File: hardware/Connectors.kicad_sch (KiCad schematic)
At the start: 23 parts, among them J1 USB_C_Receptacle_USB2.0, J14 Conn_01x05, J2 M80-5302642, J3 M300-MV31045M1, J4 M80-5L10442MC, J5 M80-5L10442MC, J6 M80-5L10442MC, J7 M80-5L10442MC

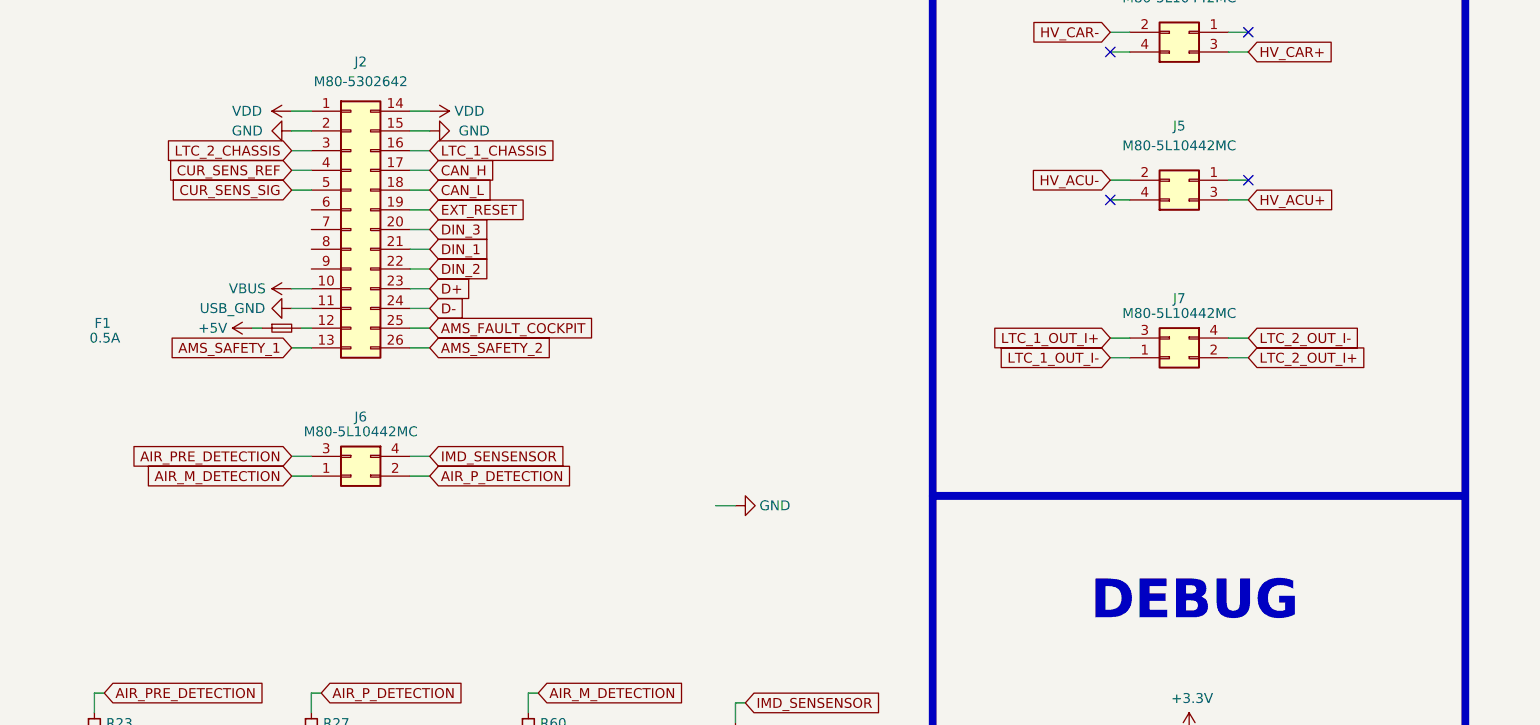
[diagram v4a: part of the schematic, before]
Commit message: bigger board, distinct HV/LV and isolation, some schematic changes
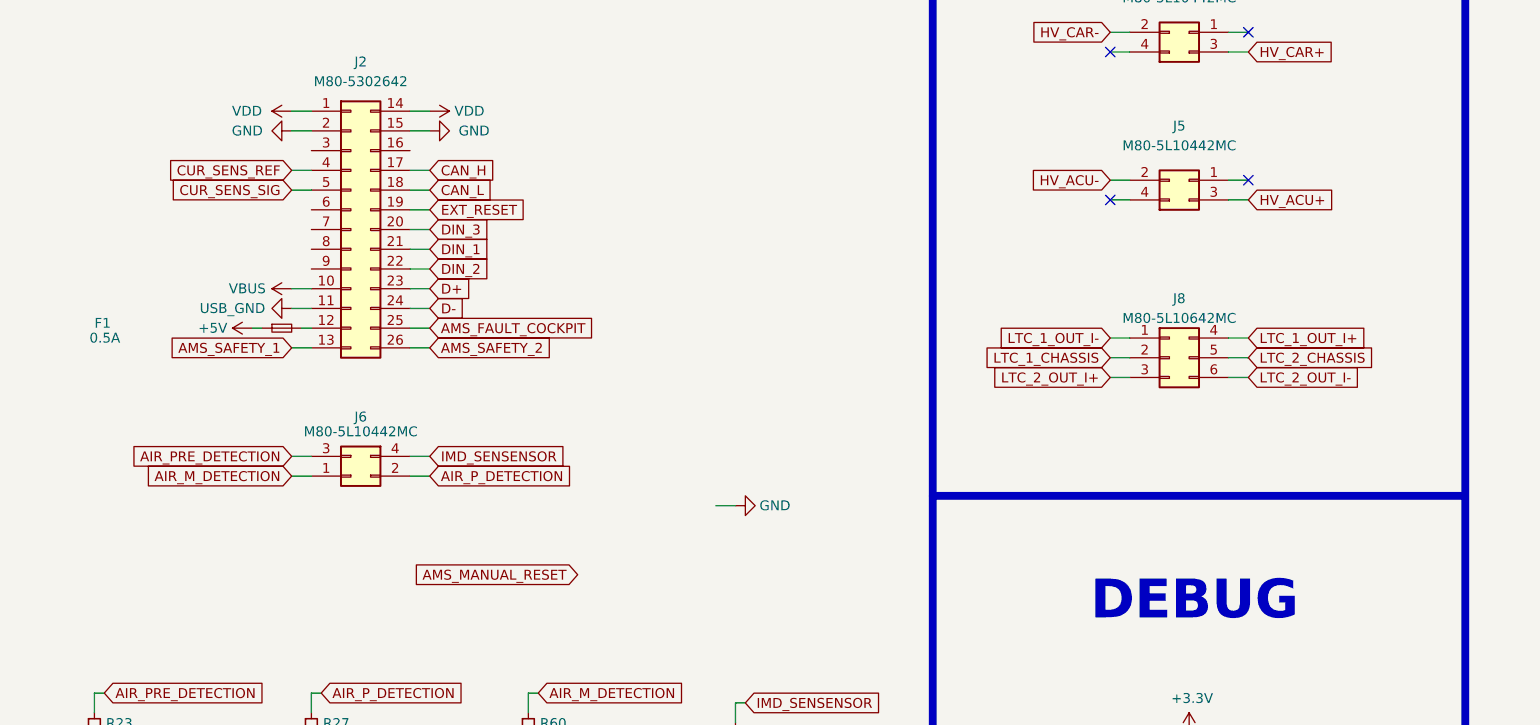
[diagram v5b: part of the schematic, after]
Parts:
- removed J7: M80-5L10442MC, M80-5L104YYMC, symbol M80-5L10442MC:M80-5L10442MC
- added J8: M80-5L10642MC, M80-5L10642MC:M80-5L106YYMC, symbol M80-5L10642MC:M80-5L10642MC
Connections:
- net LTC_1_CHASSIS: now also J8.2; no longer J2.16
- net LTC_1_OUT_I+: now also J8.4
- net LTC_1_OUT_I-: now also J8.1
- net LTC_2_CHASSIS: now also J8.5; no longer J2.3
- net LTC_2_OUT_I+: now also J8.3
- net LTC_2_OUT_I-: now also J8.6
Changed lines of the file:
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@@
     (stroke (width 0) (type default))
   )
-  (wire (pts (xy 170.18 83.82) (xy 172.72 83.82))
+  (wire (pts (xy 170.18 81.28) (xy 172.72 81.28))
     (stroke (width 0) (type default))
   )
@@
     (stroke (width 0) (type default))
   )
-  (wire (pts (xy 64.77 57.15) (xy 67.31 57.15))
+  (wire (pts (xy 187.96 83.82) (xy 185.42 83.82))
     (stroke (width 0) (type default))
   )
@@
     (stroke (width 0) (type default))
   )
-  (wire (pts (xy 187.96 81.28) (xy 185.42 81.28))
+  (wire (pts (xy 187.96 86.36) (xy 185.42 86.36))
     (stroke (width 0) (type default))
   )
@@
     (stroke (width 0) (type default))
   )
-  (wire (pts (xy 170.18 81.28) (xy 172.72 81.28))
+  (wire (pts (xy 187.96 81.28) (xy 185.42 81.28))
     (stroke (width 0) (type default))
   )
@@
     (stroke (width 0) (type default))
   )
-  (wire (pts (xy 82.55 57.15) (xy 80.01 57.15))
+  (wire (pts (xy 170.18 83.82) (xy 172.72 83.82))
     (stroke (width 0) (type default))
   )
@@
     (stroke (width 0) (type default))
   )
-  (wire (pts (xy 187.96 83.82) (xy 185.42 83.82))
+  (wire (pts (xy 170.18 86.36) (xy 172.72 86.36))
     (stroke (width 0) (type default))
   )
@@
     )
   )
-  (global_label "LTC_1_OUT_I-" (shape input) (at 170.18 83.82 180) (fields_autoplaced)
-    (effects (font (size 1.27 1.27)) (justify right))
-    (property "Intersheetrefs" "${INTERSHEET_REFS}" (at 154.7446 83.82 0)
-      (effects (font (size 1.27 1.27)) (justify right) hide)
-    )
-  )
-  (global_label "LTC_1_CHASSIS" (shape input) (at 82.55 57.15 0) (fields_autoplaced)
-    (effects (font (size 1.27 1.27)) (justify left))
-    (property "Intersheetrefs" "${INTERSHEET_REFS}" (at 99.2071 57.2294 0)
-      (effects (font (size 1.27 1.27)) (justify left) hide)
+  (global_label "LTC_1_OUT_I-" (shape input) (at 170.18 81.28 180) (fields_autoplaced)
+    (effects (font (size 1.27 1.27)) (justify right))
+    (property "Intersheetrefs" "${INTERSHEET_REFS}" (at 154.7446 81.28 0)
+      (effects (font (size 1.27 1.27)) (justify right) hide)
+    )
+  )
+  (global_label "LTC_1_CHASSIS" (shape input) (at 170.18 83.82 180) (fields_autoplaced)
+    (effects (font (size 1.27 1.27)) (justify right))
+    (property "Intersheetrefs" "${INTERSHEET_REFS}" (at 153.5956 83.82 0)
+      (effects (font (size 1.27 1.27)) (justify right) hide)
     )
   )
@@
     )
   )
+  (global_label "AMS_MANUAL_RESET" (shape input) (at 101.6 111.76 180) (fields_autoplaced)
+    (effects (font (size 1.27 1.27)) (justify right))
+    (property "Intersheetrefs" "${INTERSHEET_REFS}" (at 80.6009 111.76 0)
+      (effects (font (size 1.27 1.27)) (justify right) hide)
+    )
+  )
   (global_label "DIN_1" (shape input) (at 82.55 69.85 0) (fields_autoplaced)
     (effects (font (size 1.27 1.27)) (justify left))
@@
     )
   )
-  (global_label "LTC_2_OUT_I+" (shape input) (at 187.96 83.82 0) (fields_autoplaced)
-    (effects (font (size 1.27 1.27)) (justify left))
-    (property "Intersheetrefs" "${INTERSHEET_REFS}" (at 203.3954 83.82 0)
-      (effects (font (size 1.27 1.27)) (justify left) hide)
+  (global_label "LTC_2_OUT_I+" (shape input) (at 170.18 86.36 180) (fields_autoplaced)
+    (effects (font (size 1.27 1.27)) (justify right))
+    (property "Intersheetrefs" "${INTERSHEET_REFS}" (at 154.7446 86.36 0)
+      (effects (font (size 1.27 1.27)) (justify right) hide)
     )
   )
@@
     )
   )
-  (global_label "LTC_1_OUT_I+" (shape input) (at 170.18 81.28 180) (fields_autoplaced)
-    (effects (font (size 1.27 1.27)) (justify right))
-    (property "Intersheetrefs" "${INTERSHEET_REFS}" (at 154.7446 81.28 0)
-      (effects (font (size 1.27 1.27)) (justify right) hide)
+  (global_label "LTC_1_OUT_I+" (shape input) (at 187.96 81.28 0) (fields_autoplaced)
+    (effects (font (size 1.27 1.27)) (justify left))
+    (property "Intersheetrefs" "${INTERSHEET_REFS}" (at 203.3954 81.28 0)
+      (effects (font (size 1.27 1.27)) (justify left) hide)
     )
   )
@@
     )
   )
-  (global_label "LTC_2_CHASSIS" (shape input) (at 64.77 57.15 180) (fields_autoplaced)
-    (effects (font (size 1.27 1.27)) (justify right))
-    (property "Intersheetrefs" "${INTERSHEET_REFS}" (at 48.1129 57.0706 0)
-      (effects (font (size 1.27 1.27)) (justify right) hide)
+  (global_label "LTC_2_CHASSIS" (shape input) (at 187.96 83.82 0) (fields_autoplaced)
+    (effects (font (size 1.27 1.27)) (justify left))
+    (property "Intersheetrefs" "${INTERSHEET_REFS}" (at 204.5444 83.82 0)
+      (effects (font (size 1.27 1.27)) (justify left) hide)
     )
   )
@@
     )
   )
-  (global_label "LTC_2_OUT_I-" (shape input) (at 187.96 81.28 0) (fields_autoplaced)
-    (effects (font (size 1.27 1.27)) (justify left))
-    (property "Intersheetrefs" "${INTERSHEET_REFS}" (at 203.3954 81.28 0)
+  (global_label "LTC_2_OUT_I-" (shape input) (at 187.96 86.36 0) (fields_autoplaced)
+    (effects (font (size 1.27 1.27)) (justify left))
+    (property "Intersheetrefs" "${INTERSHEET_REFS}" (at 203.3954 86.36 0)
       (effects (font (size 1.27 1.27)) (justify left) hide)
     )
@@
         (path "/b456cffc-d9d7-4c91-91f2-36ec9a65dd1b/568caa85-d8c4-4885-aabf-c5422dff8b33"
           (reference "#PWR0122") (unit 1)
+        )
+      )
+    )
+  )
+  (symbol (lib_id "M80-5L10642MC:M80-5L10642MC") (at 179.07 83.82 0) (unit 1)
+    (in_bom yes) (on_board yes) (dnp no) (fields_autoplaced)
+    (property "Reference" "J8" (at 179.07 76.2 0)
+      (effects (font (size 1.27 1.27)))
+    )
+    (property "Value" "M80-5L10642MC" (at 179.07 78.74 0)
+      (effects (font (size 1.27 1.27)))
+    )
+    (property "Footprint" "M80-5L10642MC:M80-5L106YYMC" (at 195.58 178.74 0)
+      (effects (font (size 1.27 1.27)) (justify left top) hide)
+    )
+    (property "Datasheet" "https://cdn.harwin.com/pdfs/M80-5L1XXXXMC.pdf" (at 195.58 278.74 0)
+      (effects (font (size 1.27 1.27)) (justify left top) hide)
+    )
+    (property "Height" "" (at 195.58 478.74 0)
+      (effects (font (size 1.27 1.27)) (justify left top) hide)
+    )
+    (property "Mouser Part Number" "855-M80-5L10642MC" (at 195.58 578.74 0)
+      (effects (font (size 1.27 1.27)) (justify left top) hide)
+    )
+    (property "Mouser Price/Stock" "https://www.mouser.co.uk/ProductDetail/Harwin/M80-5L10642MC?qs=7o0qgsFWxcatGHd%2FG55JTg%3D%3D" (at 195.58 678.74 0)
+      (effects (font (size 1.27 1.27)) (justify left top) hide)
+    )
+    (property "Manufacturer_Name" "Harwin" (at 195.58 778.74 0)
+      (effects (font (size 1.27 1.27)) (justify left top) hide)
+    )
+    (property "Manufacturer_Part_Number" "M80-5L10642MC" (at 195.58 878.74 0)
+      (effects (font (size 1.27 1.27)) (justify left top) hide)
+    )
+    (pin "1")
+    (pin "2")
+    (pin "3")
+    (pin "4")
+    (pin "5")
+    (pin "6")
+    (instances
+      (project "PUTM_EV_BMS_HV_Master_2021"
+        (path "/b456cffc-d9d7-4c91-91f2-36ec9a65dd1b/568caa85-d8c4-4885-aabf-c5422dff8b33"
+          (reference "J8") (unit 1)
         )
       )
@@
         )
       )
-    )
-  )
-  (symbol (lib_id "M80-5L10442MC:M80-5L10442MC") (at 179.07 82.55 180) (unit 1)
-    (in_bom yes) (on_board yes) (dnp no)
-    (property "Reference" "J7" (at 179.07 76.2 0)
-      (effects (font (size 1.27 1.27)))
-    )
-    (property "Value" "M80-5L10442MC" (at 179.07 78.105 0)
-      (effects (font (size 1.27 1.27)))
-    )
-    (property "Footprint" "M80-5L104YYMC" (at 162.56 85.09 0)
-      (effects (font (size 1.27 1.27)) (justify left) hide)
-    )
-    (property "Datasheet" "https://cdn.harwin.com/pdfs/M80-5L1XXXXMC.pdf" (at 162.56 82.55 0)
-      (effects (font (size 1.27 1.27)) (justify left) hide)
-    )
-    (property "Description" "Datamate J-Tek DIL Male Horizontal 3mm Throughboard Connector, selective gold + tin, retainers for 101Lok, 2+2 contacts" (at 162.56 80.01 0)
-      (effects (font (size 1.27 1.27)) (justify left) hide)
-    )
-    (property "Height" "" (at 162.56 77.47 0)
-      (effects (font (size 1.27 1.27)) (justify left) hide)
-    )
-    (property "Mouser Part Number" "855-M80-5L10442MC" (at 162.56 74.93 0)
-      (effects (font (size 1.27 1.27)) (justify left) hide)
-    )
-    (property "Mouser Price/Stock" "https://www.mouser.co.uk/ProductDetail/Harwin/M80-5L10442MC?qs=Ep9Lwju7gVqLc8wvBnHi3A%3D%3D" (at 162.56 72.39 0)
-      (effects (font (size 1.27 1.27)) (justify left) hide)
-    )
-    (property "Manufacturer_Name" "Harwin" (at 162.56 69.85 0)
-      (effects (font (size 1.27 1.27)) (justify left) hide)
-    )
-    (property "Manufacturer_Part_Number" "M80-5L10442MC" (at 162.56 67.31 0)
-      (effects (font (size 1.27 1.27)) (justify left) hide)
-    )
-    (pin "1")
-    (pin "2")
-    (pin "3")
-    (pin "4")
-    (instances
-      (project "PUTM_EV_BMS_HV_Master_2021"
-        (path "/b456cffc-d9d7-4c91-91f2-36ec9a65dd1b/568caa85-d8c4-4885-aabf-c5422dff8b33"
-          (reference "J7") (unit 1)
-        )
-      )
